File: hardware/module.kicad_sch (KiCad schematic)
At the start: 40 parts, among them J2 PROG, J3 PRB1, J4 PRB2, P1 USB_C_Plug_USB2.0, SW1 RESET, U1 STM32L010C6Tx, U2 CP2102N-Axx-xQFN20, U3 USBLC6-2P6, U4 TMUX6236, U5 EZO-EC™, U6 SI8600AB-B-IS, U7 TPS631000

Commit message: Update PCB module design
Co-authored-by: Kshitij Dadhekar <kshitij.dadhekar@clearwings.nl>
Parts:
- removed J2: PROG, Connector:Tag-Connect_TC2030-IDC-NL_2x03_P1.27mm_Vertical, symbol Connector:Conn_ARM_SWD_TagConnect_TC2030-NL
- removed J3: PRB1, Connector_Coaxial:SMA_Molex_73251-1153_EdgeMount_Horizontal, symbol Connector:Conn_Coaxial
- removed J4: PRB2, Connector_Coaxial:SMA_Molex_73251-1153_EdgeMount_Horizontal, symbol Connector:Conn_Coaxial
- removed PS1: IA0505S, Converter_DCDC:Converter_DCDC_XP_POWER-IAxxxxS_THT, symbol Converter_DCDC:IA0505S
- removed U3: USBLC6-2P6, Package_TO_SOT_SMD:SOT-666, symbol Power_Protection:USBLC6-2P6
- removed U6: SI8600AB-B-IS, Package_SO:SOIC-8_3.9x4.9mm_P1.27mm, symbol SI8600:SI8600AB-B-IS
- added C12, C13, C14, C15: 100n, Capacitor_SMD:C_0603_1608Metric, symbol Device:C_Small
- added C16, C17, C19, C21: 4u7, Capacitor_SMD:C_0603_1608Metric, symbol Device:C_Small
- added C18, C20: 47u, Capacitor_SMD:C_0805_2012Metric, symbol Device:C_Small
- added C22, C23: 10u, Capacitor_SMD:C_0603_1608Metric, symbol Device:C_Small
- added D1, D2, D3, D4: MBR0520LT1G, Diode_SMD:D_SOD-123, symbol Diode:MBR0520
- added FID1, FID2: Fiducial, Fiducial:Fiducial_0.5mm_Mask1mm, symbol Mechanical:Fiducial
- added J1: Conn_ARM_JTAG_SWD_10, Connector:Tag-Connect_TC2050-IDC-NL_2x05_P1.27mm_Vertical, symbol Connector:Conn_ARM_JTAG_SWD_10
- added J3: 1725698, TerminalBlock_Phoenix:TerminalBlock_Phoenix_MPT-0,5-6-2.54_1x06_P2.54mm_Horizontal, symbol Connector:Screw_Terminal_01x06
- added J6, J7: CON-SMA-EDGE-S, CON-SMA-EDGE-S:RFSOLUTIONS_CON-SMA-EDGE-S, symbol CON-SMA-EDGE-S:CON-SMA-EDGE-S
- added PS1: IA0505D, Converter_DCDC:Converter_DCDC_XP_POWER-IAxxxxD_THT, symbol Converter_DCDC:IA0505D
- added R15, R16: 2K2, Resistor_SMD:R_0603_1608Metric, symbol Device:R_Small
- added R17, R18, R19, R20, R21, R22: 0R, Resistor_SMD:R_0603_1608Metric, symbol Device:R_Small
- added R23: 10k, Resistor_SMD:R_0603_1608Metric, symbol Device:R_Small
- added R24, R25: 5k2, Resistor_SMD:R_0603_1608Metric, symbol Device:R_Small
- added TP1, TP10, TP11, TP12, TP13, TP14, TP15, TP16, TP2, TP3, TP4, TP5, TP6, TP7, TP8, TP9: TestPoint, TestPoint:TestPoint_Pad_1.0x1.0mm, symbol Connector:TestPoint
- added U3: USBLC6-2P6, USBLC6-2P6:SOT50P160X60-6N, symbol USBLC6:USBLC6-2P6
- added U6: ISO1644DWR, Package_SO:SOIC-16W_7.5x10.3mm_P1.27mm, symbol Isolator:ISO1644DWR
- C1: value 100n -> 4u7; footprint Capacitor_SMD:C_0805_2012Metric -> Capacitor_SMD:C_0603_1608Metric
- C10, C11, C3, C4, C5, C6, C7, C8, C9: footprint Capacitor_SMD:C_0805_2012Metric -> Capacitor_SMD:C_0603_1608Metric
- C2: value 47u -> 10u; footprint Capacitor_SMD:C_0805_2012Metric -> Capacitor_SMD:C_0603_1608Metric
- JP1: now not fitted
- L1: value 1uH @ 2.1A -> LPWI201208S1R0T
- P1: value USB_C_Plug_USB2.0 -> USB4105-GF-A
- R1, R10, R11, R12, R13, R14, R2, R3, R4, R5, R6, R7, R9: footprint Resistor_SMD:R_0805_2012Metric -> Resistor_SMD:R_0603_1608Metric
- R8: value 27 -> 10k; footprint Resistor_SMD:R_0805_2012Metric -> Resistor_SMD:R_0603_1608Metric
- SW1: value RESET -> PTS810SJG250SMTRLFS; footprint Button_Switch_SMD:SW_SPST_CK_RS282G05A3 -> Button_Switch_SMD:SW_SPST_PTS810
- U1: value STM32L010C6Tx -> STM32L010C6T6
- U2: value CP2102N-Axx-xQFN20 -> CP2102N-A02-GQFN20
- U4: value TMUX6236 -> TMUX6236PWR
- U5: now not fitted; now left out of the parts list
- U7: value TPS631000 -> TPS631000DRLR
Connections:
- net PRB_SEL_B is gone; now on net PRB_SEL: U4.9 (SEL2)
- net +5V: now also D3.2 (A), TP11.1
- net +5V_ISO: now also R8.2, C13.1, C15.1, C17.1, J3.1 (Pin_1), J3.4 (Pin_4), PS1.5 (+Vout), R24.2, R25.2, TP8.1, U6.16 (VCC2)
- net -5V_ISO: now also C12.1, C14.2, C16.2, PS1.4 (-Vout), TP10.1
- net BOOST_EN: now also R22.1, R23.1
- net GND: now also C18.2, C19.2, C20.2, C21.2, C22.2, C23.2, J1.3 (GND), J1.5 (GND), PS1.1 (-Vin), R23.2, TP12.1, U3.2, U6.2 (GND1), U6.8 (GND1)
- net GND_ISO: now also C12.2, C13.2, C14.1, C15.2, C16.1, C17.2, J3.3 (Pin_3), J3.6 (Pin_6), PS1.6 (0V), TP9.1, U6.15 (GND2), U6.9 (GND2)
- net I2C_SCL: now also R16.2, R17.1; no longer U1.42 (PB6)
- net I2C_SDA: now also R15.2, R18.1; no longer U1.43 (PB7)
- net LPUART1_RX: now also R11.1, U6.7 (OUT); no longer R11.2
- net LPUART1_TX: now also R10.1, U6.5 (INB); no longer R10.2
- net MOD_ID1: now also R19.1
- net MOD_ID2: now also R20.1
- net MOD_ID3: now also R21.1
- net NRST: now also J1.10 (~{RESET})
- net SWCLK: now also J1.4 (SWCLK/TCK)
- net SWDIO: now also J1.2 (SWDIO/TMS)
- net VSensor: now also D1.2 (A), TP3.1; no longer C10.1, C11.1, C4.1, C7.1, C8.1, C9.1, JP1.2 (B), R10.1, R11.1, R8.2, U1.24 (VDD), U1.36 (VDD), U1.48 (VDD), U1.9 (VDDA)
- net DQ_TEMP_A: now reaches U1.15 (PA5)
- net DQ_TEMP_A: now also TP14.1, U6.3 (SDA1)
- net PRB_SEL_MCU: now reaches U1.16 (PA6)
- net PRB_SEL_MCU: now also U6.4 (INA)
- net DQ_TEMP_B: now reaches U1.17 (PA7)
- net DQ_TEMP_B: now also TP13.1, U6.6 (SCL1)
- net at U1.25 (PB12): now also R22.2
- net at U1.41 (PB5): now also R20.2
- net at U1.45 (PB8): now also R21.2
- net at U1.46 (PB9): now also R19.2
- net 3V3: now reaches C3.1, U7.4 (Vin)
- net 3V3: now also C10.1, C11.1, C4.1, C7.1, C8.1, C9.1, JP1.2 (B), R10.2, R11.2, U1.24 (VDD), U1.36 (VDD), U1.48 (VDD), U1.9 (VDDA), C23.1, D1.1 (K), D2.1 (K), J1.1 (VTref), R15.1, R16.1, TP4.1, U6.1 (VCC1); no longer R8.1
- net CP2102_3V3: now reaches R3.2, U2.6 (VDD)
- net CP2102_3V3: now also C20.1, C21.1, D2.2 (A), TP2.1
- net at R12.2: now also U5.2 (TX/SDA), U6.10 (INC); no longer U5.1 (RX/SCL)
- net CP_N: now reaches U2.5 (D-)
- net CP_N: now also U3.1
- net CP_P: now reaches U2.4 (D+)
- net CP_P: now also U3.3
- net USB_P: now reaches P1.A6 (D+)
- net USB_P: now also P1.B6 (D+), U3.4
- net USB_VBUS: now reaches P1.A4 (VBUS), P1.A9 (VBUS), P1.B4 (VBUS), P1.B9 (VBUS), R4.2, U2.7 (VREGIN)
- net USB_VBUS: now also C18.1, C19.1, D4.2 (A), TP1.1, U3.5
- net USB_N: now reaches P1.A7 (D-)
- net USB_N: now also P1.B7 (D-), U3.6
- net at R13.2: now also U5.1 (RX/SCL), U6.12 (OUTB); no longer U5.2 (TX/SDA)
- net at U4.11 (D2), U5.4 (PRB): now also TP6.1
- net at U4.3 (D1), U5.5 (PRB): now also TP5.1
- net at U4.4 (S1B): now also J7.1
- net at U4.12 (S2B): now also J7.G1, J7.G2, J7.G3, J7.G4
- net at U4.10 (S2A): now also J6.G1, J6.G2, J6.G3, J6.G4
- net at U4.2 (S1A): now also J6.1
- net PRB_EN: no longer names the net of U4.14 (EN)
- net PRB_EN: now also R8.1
- net PRB_SEL_A renamed PRB_SEL
- net PRB_SEL: now also U6.13 (OUTA)
- new net: R17.2, U1.42 (PB6)
- new net: R18.2, U1.43 (PB7)
- new net: C22.1, D3.1 (K), D4.1 (K), PS1.3 (+Vin), TP7.1
- new net DQ_TEMP_A_ISO: J3.5 (Pin_5), R24.1, TP16.1, U6.14 (SDA2)
- new net DQ_TEMP_B_ISO: J3.2 (Pin_2), R25.1, TP15.1, U6.11 (SCL2)
- no-connect marks 32 -> 34
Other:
- note added: "5-10mA"
- note added: "50mA max."
- note added: "76uA per MHz 32mA max."
- note added: "Dual power supply support"
- moved on the sheet: C1, C2, C3, C4, C5, R10, R11, R12, R13, R14, R3, R4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

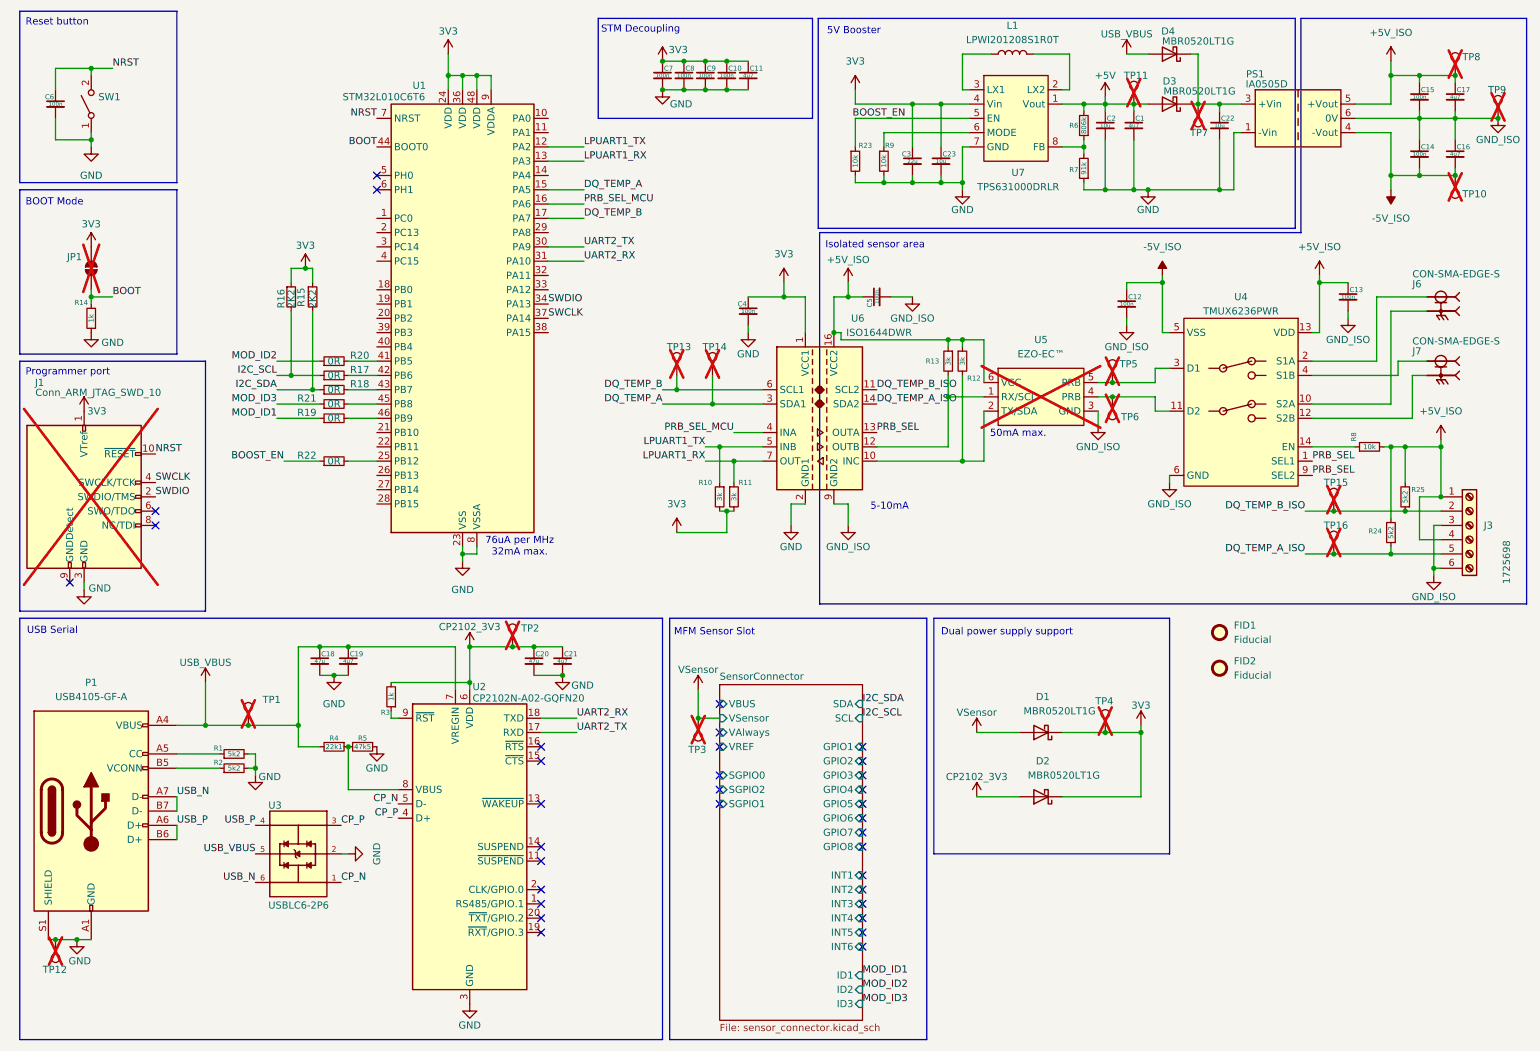
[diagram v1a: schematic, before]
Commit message: feat: new shell commands chore: remove saul pins chore: add compile time FW_VERSION docs: add calibration interpolated graphs
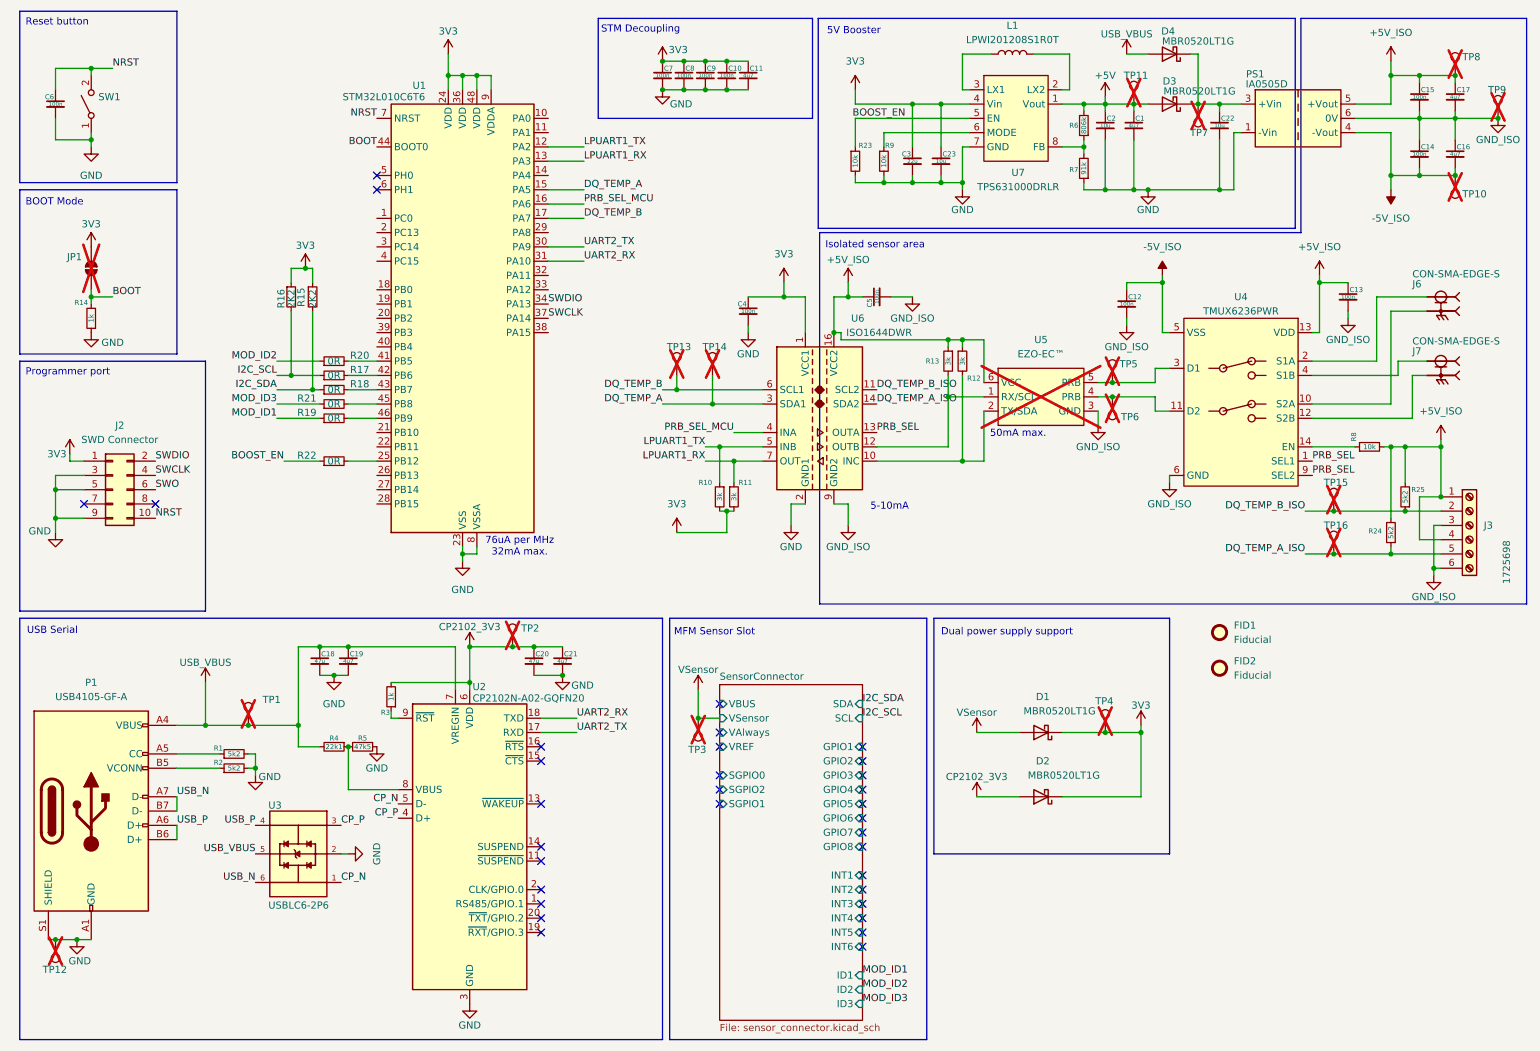
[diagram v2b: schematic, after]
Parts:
- removed J1: Conn_ARM_JTAG_SWD_10, Connector:Tag-Connect_TC2050-IDC-NL_2x05_P1.27mm_Vertical, symbol Connector:Conn_ARM_JTAG_SWD_10
- added J2: SWD Connector, Connector_PinHeader_1.27mm:PinHeader_2x05_P1.27mm_Vertical, symbol Connector_Generic:Conn_02x05_Odd_Even
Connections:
- net 3V3: now also J2.1 (Pin_1)
- net GND: now also J2.3 (Pin_3), J2.5 (Pin_5), J2.9 (Pin_9)
- net NRST: now also J2.10 (Pin_10)
- net SWCLK: now also J2.4 (Pin_4)
- net SWDIO: now also J2.2 (Pin_2)
- new net SWO: J2.6 (Pin_6)
- no-connect marks 34 -> 33
